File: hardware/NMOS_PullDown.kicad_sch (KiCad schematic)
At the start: 3 parts, among them Q2 2N7002

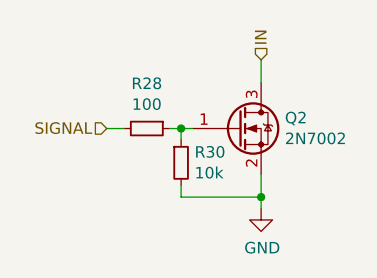
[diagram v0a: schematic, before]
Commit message: finished remaking whole schematic
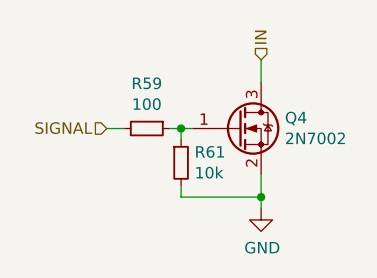
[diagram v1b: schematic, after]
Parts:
- renumbered Q2 to Q4, R28 to R59, R30 to R61
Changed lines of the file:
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@@
   (symbol (lib_id "Transistor_FET:2N7002") (at 145.415 94.615 0)
     (in_bom yes) (on_board yes)
-    (property "Reference" "Q2" (id 0) (at 150.5966 93.4466 0)
+    (property "Reference" "Q4" (id 0) (at 150.5966 93.4466 0)
       (effects (font (size 1.27 1.27)) (justify left))
     )
@@
   (symbol (lib_id "Device:R_Small") (at 139.065 98.425 0)
     (in_bom yes) (on_board yes)
-    (property "Reference" "R30" (id 0) (at 140.5636 97.2566 0)
+    (property "Reference" "R61" (id 0) (at 140.5636 97.2566 0)
       (effects (font (size 1.27 1.27)) (justify left))
     )
@@
   (symbol (lib_id "Device:R_Small") (at 135.255 94.615 270)
     (in_bom yes) (on_board yes)
-    (property "Reference" "R28" (id 0) (at 135.255 89.6366 90))
+    (property "Reference" "R59" (id 0) (at 135.255 89.6366 90))
     (property "Value" "100" (id 1) (at 135.255 91.948 90))
     (property "Footprint" "Resistor_SMD:R_0603_1608Metric" (id 2) (at 135.255 94.615 0)

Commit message: added additional USB port and overall board update
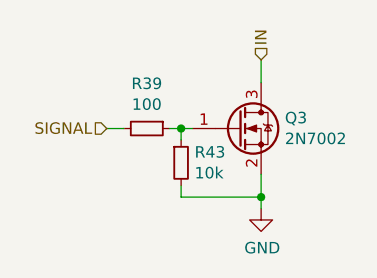
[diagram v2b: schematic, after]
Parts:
- renumbered Q4 to Q3, R59 to R39, R61 to R43
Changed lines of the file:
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@@
   (symbol (lib_id "Transistor_FET:2N7002") (at 145.415 94.615 0)
     (in_bom yes) (on_board yes)
-    (property "Reference" "Q4" (id 0) (at 150.5966 93.4466 0)
+    (property "Reference" "Q3" (id 0) (at 150.5966 93.4466 0)
       (effects (font (size 1.27 1.27)) (justify left))
     )
@@
   (symbol (lib_id "Device:R_Small") (at 139.065 98.425 0)
     (in_bom yes) (on_board yes)
-    (property "Reference" "R61" (id 0) (at 140.5636 97.2566 0)
+    (property "Reference" "R43" (id 0) (at 140.5636 97.2566 0)
       (effects (font (size 1.27 1.27)) (justify left))
     )
@@
   (symbol (lib_id "Device:R_Small") (at 135.255 94.615 270)
     (in_bom yes) (on_board yes)
-    (property "Reference" "R59" (id 0) (at 135.255 89.6366 90))
+    (property "Reference" "R39" (id 0) (at 135.255 89.6366 90))
     (property "Value" "100" (id 1) (at 135.255 91.948 90))
     (property "Footprint" "Resistor_SMD:R_0603_1608Metric" (id 2) (at 135.255 94.615 0)
@@
   (symbol (lib_id "power:GND") (at 147.955 103.505 0)
     (in_bom yes) (on_board yes)
-    (property "Reference" "#PWR?" (id 0) (at 147.955 109.855 0)
+    (property "Reference" "#PWR0132" (id 0) (at 147.955 109.855 0)
       (effects (font (size 1.27 1.27)) hide)
     )

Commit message: switched all screw terminals for corresponding molexes n-pins 90 deg
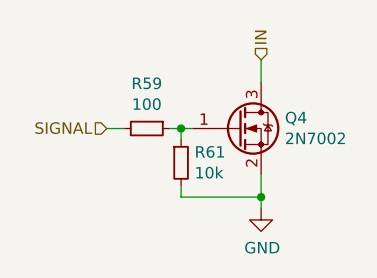
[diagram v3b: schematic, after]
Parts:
- renumbered Q3 to Q4, R39 to R59, R43 to R61
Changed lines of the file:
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@@
   (symbol (lib_id "Transistor_FET:2N7002") (at 145.415 94.615 0)
     (in_bom yes) (on_board yes)
-    (property "Reference" "Q3" (id 0) (at 150.5966 93.4466 0)
+    (property "Reference" "Q4" (id 0) (at 150.5966 93.4466 0)
       (effects (font (size 1.27 1.27)) (justify left))
     )
@@
   (symbol (lib_id "Device:R_Small") (at 139.065 98.425 0)
     (in_bom yes) (on_board yes)
-    (property "Reference" "R43" (id 0) (at 140.5636 97.2566 0)
+    (property "Reference" "R61" (id 0) (at 140.5636 97.2566 0)
       (effects (font (size 1.27 1.27)) (justify left))
     )
@@
   (symbol (lib_id "Device:R_Small") (at 135.255 94.615 270)
     (in_bom yes) (on_board yes)
-    (property "Reference" "R39" (id 0) (at 135.255 89.6366 90))
+    (property "Reference" "R59" (id 0) (at 135.255 89.6366 90))
     (property "Value" "100" (id 1) (at 135.255 91.948 90))
     (property "Footprint" "Resistor_SMD:R_0603_1608Metric" (id 2) (at 135.255 94.615 0)
@@
   (symbol (lib_id "power:GND") (at 147.955 103.505 0)
     (in_bom yes) (on_board yes)
-    (property "Reference" "#PWR0132" (id 0) (at 147.955 109.855 0)
+    (property "Reference" "#PWR0129" (id 0) (at 147.955 109.855 0)
       (effects (font (size 1.27 1.27)) hide)
     )

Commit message: sync
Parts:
- renumbered Q4 to Q1, R59 to R17, R61 to R22
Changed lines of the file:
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@@
   (symbol (lib_id "Transistor_FET:2N7002") (at 145.415 94.615 0)
     (in_bom yes) (on_board yes)
-    (property "Reference" "Q4" (id 0) (at 150.5966 93.4466 0)
+    (property "Reference" "Q1" (id 0) (at 150.5966 93.4466 0)
       (effects (font (size 1.27 1.27)) (justify left))
     )
@@
   (symbol (lib_id "Device:R_Small") (at 139.065 98.425 0)
     (in_bom yes) (on_board yes)
-    (property "Reference" "R61" (id 0) (at 140.5636 97.2566 0)
+    (property "Reference" "R22" (id 0) (at 140.5636 97.2566 0)
       (effects (font (size 1.27 1.27)) (justify left))
     )
@@
   (symbol (lib_id "Device:R_Small") (at 135.255 94.615 270)
     (in_bom yes) (on_board yes)
-    (property "Reference" "R59" (id 0) (at 135.255 89.6366 90))
+    (property "Reference" "R17" (id 0) (at 135.255 89.6366 90))
     (property "Value" "100" (id 1) (at 135.255 91.948 90))
     (property "Footprint" "Resistor_SMD:R_0603_1608Metric" (id 2) (at 135.255 94.615 0)

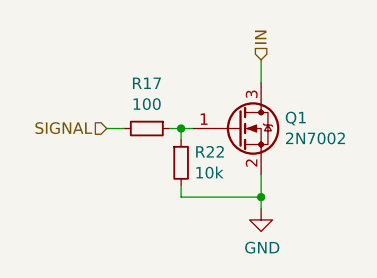
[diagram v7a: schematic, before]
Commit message: remade pcb so it fits into 100 x 100 mm and some minor modifications
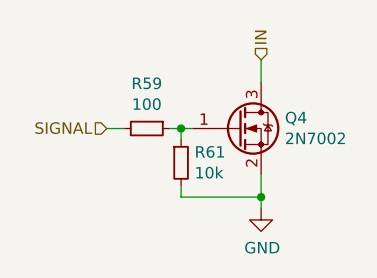
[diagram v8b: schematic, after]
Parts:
- renumbered Q1 to Q4, R17 to R59, R22 to R61
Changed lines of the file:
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@@
   (symbol (lib_id "Transistor_FET:2N7002") (at 145.415 94.615 0)
     (in_bom yes) (on_board yes)
-    (property "Reference" "Q1" (id 0) (at 150.5966 93.4466 0)
+    (property "Reference" "Q4" (id 0) (at 150.5966 93.4466 0)
       (effects (font (size 1.27 1.27)) (justify left))
     )
@@
   (symbol (lib_id "Device:R_Small") (at 139.065 98.425 0)
     (in_bom yes) (on_board yes)
-    (property "Reference" "R22" (id 0) (at 140.5636 97.2566 0)
+    (property "Reference" "R61" (id 0) (at 140.5636 97.2566 0)
       (effects (font (size 1.27 1.27)) (justify left))
     )
@@
   (symbol (lib_id "Device:R_Small") (at 135.255 94.615 270)
     (in_bom yes) (on_board yes)
-    (property "Reference" "R17" (id 0) (at 135.255 89.6366 90))
+    (property "Reference" "R59" (id 0) (at 135.255 89.6366 90))
     (property "Value" "100" (id 1) (at 135.255 91.948 90))
     (property "Footprint" "Resistor_SMD:R_0603_1608Metric" (id 2) (at 135.255 94.615 0)
@@
   (symbol (lib_id "power:GND") (at 147.955 103.505 0)
     (in_bom yes) (on_board yes)
-    (property "Reference" "#PWR0132" (id 0) (at 147.955 109.855 0)
+    (property "Reference" "#PWR0129" (id 0) (at 147.955 109.855 0)
       (effects (font (size 1.27 1.27)) hide)
     )
